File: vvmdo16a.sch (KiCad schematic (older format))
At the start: 18 parts, among them J1 517-N2510-6002RB, J2 517-N2520-6002RB, SW1 SW_Coded_SH-7010, U1 PCA9685PW, U2 ULN2803A, U3 ULN2803A

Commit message: More compact PCB
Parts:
- removed MK3, MK4: Mounting_Hole_PAD, Mounting_Holes:MountingHole_2.7mm_M2.5_DIN965_Pad, symbol mechanical:Mounting_Hole_PAD
- MK1, MK2: value Mounting_Hole_PAD -> M2.5
- SW1: value SW_Coded_SH-7010 -> 220ADC16
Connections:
- net A0: now reaches R1.1, SW1.1, U1.1 (A0)
- net A1: now reaches R2.1, SW1.2, U1.2 (A1)
- net A2: now reaches R3.1, SW1.4, U1.3 (A2)
- net A3: now reaches R4.1, SW1.8, U1.4 (A3)
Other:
- moved on the sheet: MK2
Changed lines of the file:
@@
 P 4250 5900
 F 0 "MK1" H 4350 5949 50  0000 L CNN
-F 1 "Mounting_Hole_PAD" H 4350 5858 50  0000 L CNN
+F 1 "M2.5" H 4350 5858 50  0000 L CNN
 F 2 "Mounting_Holes:MountingHole_2.7mm_M2.5_DIN965_Pad" H 4250 5900 50  0001 C CNN
 F 3 "" H 4250 5900 50  0001 C CNN
@@
 L mechanical:Mounting_Hole_PAD MK2
 U 1 1 5D014BC8
-P 4500 5900
-F 0 "MK2" H 4600 5949 50  0000 L CNN
-F 1 "Mounting_Hole_PAD" H 4600 5858 50  0000 L CNN
-F 2 "Mounting_Holes:MountingHole_2.7mm_M2.5_DIN965_Pad" H 4500 5900 50  0001 C CNN
-F 3 "" H 4500 5900 50  0001 C CNN
-	1    4500 5900
-	1    0    0    -1
-$EndComp
-$Comp
-L mechanical:Mounting_Hole_PAD MK3
-U 1 1 5D014C18
-P 4750 5900
-F 0 "MK3" H 4850 5949 50  0000 L CNN
-F 1 "Mounting_Hole_PAD" H 4850 5858 50  0000 L CNN
-F 2 "Mounting_Holes:MountingHole_2.7mm_M2.5_DIN965_Pad" H 4750 5900 50  0001 C CNN
-F 3 "" H 4750 5900 50  0001 C CNN
-	1    4750 5900
-	1    0    0    -1
-$EndComp
-$Comp
-L mechanical:Mounting_Hole_PAD MK4
-U 1 1 5D014E7E
-P 5000 5900
-F 0 "MK4" H 5100 5949 50  0000 L CNN
-F 1 "Mounting_Hole_PAD" H 5100 5858 50  0000 L CNN
-F 2 "Mounting_Holes:MountingHole_2.7mm_M2.5_DIN965_Pad" H 5000 5900 50  0001 C CNN
-F 3 "" H 5000 5900 50  0001 C CNN
-	1    5000 5900
+P 4550 5900
+F 0 "MK2" H 4650 5949 50  0000 L CNN
+F 1 "M2.5" H 4650 5858 50  0000 L CNN
+F 2 "Mounting_Holes:MountingHole_2.7mm_M2.5_DIN965_Pad" H 4550 5900 50  0001 C CNN
+F 3 "" H 4550 5900 50  0001 C CNN
+	1    4550 5900
 	1    0    0    -1
 $EndComp
@@
 L power:GND #PWR0107
 U 1 1 5D0210BD
-P 4650 6250
-F 0 "#PWR0107" H 4650 6000 50  0001 C CNN
-F 1 "GND" H 4655 6077 50  0000 C CNN
-F 2 "" H 4650 6250 50  0001 C CNN
-F 3 "" H 4650 6250 50  0001 C CNN
-	1    4650 6250
+P 4400 6250
+F 0 "#PWR0107" H 4400 6000 50  0001 C CNN
+F 1 "GND" H 4405 6077 50  0000 C CNN
+F 2 "" H 4400 6250 50  0001 C CNN
+F 3 "" H 4400 6250 50  0001 C CNN
+	1    4400 6250
 	1    0    0    -1
 $EndComp
 Wire Wire Line
 	4250 6000 4250 6100
-Wire Wire Line
-	4250 6100 4500 6100
-Wire Wire Line
-	4650 6100 4650 6250
-Wire Wire Line
-	4500 6000 4500 6100
-Connection ~ 4500 6100
-Wire Wire Line
-	4500 6100 4650 6100
-Wire Wire Line
-	4650 6100 4750 6100
-Wire Wire Line
-	4750 6100 4750 6000
-Connection ~ 4650 6100
-Wire Wire Line
-	4750 6100 5000 6100
-Wire Wire Line
-	5000 6100 5000 6000
-Connection ~ 4750 6100
 Wire Wire Line
 	7000 1900 8450 1900
@@
 P 1850 3750
 F 0 "SW1" H 1907 4217 50  0000 C CNN
-F 1 "SW_Coded_SH-7010" H 1907 4126 50  0000 C CNN
+F 1 "220ADC16" H 1907 4126 50  0000 C CNN
 F 2 "Buttons_Switches_THT:Nidec_Copal_SH-7010C" H 1550 3300 50  0001 L CNN
 F 3 "https://www.nidec-copal-electronics.com/e/catalog/switch/sh-7000.pdf" H 1850 3750 50  0001 C CNN
@@
 	1    0    0    -1
 $EndComp
+Text Label 3050 3650 0    50   ~ 0
+A0
+Text Label 3050 3750 0    50   ~ 0
+A1
+Text Label 3050 3850 0    50   ~ 0
+A2
+Text Label 3050 3950 0    50   ~ 0
+A3
+Wire Wire Line
+	4250 6100 4400 6100
+Wire Wire Line
+	4400 6100 4400 6250
+Wire Wire Line
+	4400 6100 4550 6100
+Wire Wire Line
+	4550 6100 4550 6000
 Wire Bus Line
 	9700 2050 9700 3450
@@
 Wire Bus Line
 	7550 2050 7550 4450
+Connection ~ 4400 6100
 $EndSCHEMATC

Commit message: Add seperate power rail input Label the board
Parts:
- added J3: Conn_02x01, Pin_Headers:Pin_Header_Straight_2x01_Pitch2.54mm, symbol conn:Conn_02x01
- added J4: Conn_02x01, TerminalBlocks_Phoenix:TerminalBlock_Phoenix_PT-3.5mm_2pol, symbol conn:Conn_02x01
- J1: value 517-N2510-6002RB -> 517-N2508-6002RB; footprint Connectors_IDC:IDC-Header_2x05_Pitch2.54mm_Straight -> Connector-IDC:IDC-Header_2x04_P2.54mm_Vertical; symbol conn:Conn_02x05_Odd_Even -> conn:Conn_02x04_Odd_Even
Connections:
- net +12V: now also J3.2 (Pin_2), J4.1 (Pin_1); no longer J1.7 (Pin_7), J1.8 (Pin_8)
- net +3V3: now also J1.5 (Pin_5), J1.6 (Pin_6); no longer J1.1 (Pin_1), J1.2 (Pin_2)
- net GND: now also J1.1 (Pin_1), J1.2 (Pin_2), J4.2 (Pin_2); no longer J1.10 (Pin_10), J1.9 (Pin_9)
- net SCL: now also J1.3 (Pin_3); no longer J1.4 (Pin_4)
- net SDA: now also J1.4 (Pin_4); no longer J1.3 (Pin_3)
- new net +12VIN: J1.7 (Pin_7), J1.8 (Pin_8), J3.1 (Pin_1)
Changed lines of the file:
@@
 O16
 $Comp
-L conn:Conn_02x05_Odd_Even J1
+L conn:Conn_02x04_Odd_Even J1
 U 1 1 5CD0D077
-P 1950 2850
-F 0 "J1" H 2000 3267 50  0000 C CNN
-F 1 "517-N2510-6002RB" H 2000 3176 50  0000 C CNN
-F 2 "Connectors_IDC:IDC-Header_2x05_Pitch2.54mm_Straight" H 1950 2850 50  0001 C CNN
-F 3 "~" H 1950 2850 50  0001 C CNN
-	1    1950 2850
-	1    0    0    -1
+P 2250 2350
+F 0 "J1" H 2300 2767 50  0000 C CNN
+F 1 "517-N2508-6002RB" H 2300 2676 50  0000 C CNN
+F 2 "Connector-IDC:IDC-Header_2x04_P2.54mm_Vertical" H 2250 2350 50  0001 C CNN
+F 3 "~" H 2250 2350 50  0001 C CNN
+	1    2250 2350
+	-1   0    0    1
 $EndComp
 Wire Wire Line
@@
 $EndComp
 Wire Wire Line
-	3950 1750 3950 2000
-Wire Wire Line
-	3250 2750 2250 2750
-Wire Wire Line
-	3250 2850 2750 2850
-Wire Wire Line
-	2750 2850 2750 2350
-Wire Wire Line
-	2750 2350 1550 2350
-Wire Wire Line
-	1550 2350 1550 2750
-Wire Wire Line
-	1550 2750 1750 2750
-Wire Wire Line
-	1750 2650 1350 2650
-Wire Wire Line
-	1350 2650 1350 2000
-Wire Wire Line
-	1350 2000 2450 2000
-Connection ~ 3950 2000
-Wire Wire Line
-	3950 2000 3950 2450
-Wire Wire Line
 	3250 4150 3150 4150
 Wire Wire Line
@@
 Connection ~ 2700 4950
 Wire Wire Line
-	2250 2650 2450 2650
-Wire Wire Line
-	2450 2650 2450 2000
-Connection ~ 2450 2000
-Wire Wire Line
-	2450 2000 3950 2000
-Wire Wire Line
-	2250 3050 2350 3050
-Wire Wire Line
 	2350 3050 2350 4950
 Wire Wire Line
@@
 Connection ~ 2550 4950
 Wire Wire Line
-	1750 3050 1450 3050
-Wire Wire Line
-	1450 3050 1450 4950
-Wire Wire Line
 	1450 4950 2350 4950
 Connection ~ 2350 4950
-Wire Wire Line
-	2250 2950 2550 2950
-Wire Wire Line
-	2550 2950 2550 1900
-Wire Wire Line
-	2550 1900 1450 1900
-Wire Wire Line
-	1450 1900 1450 2950
-Wire Wire Line
-	1450 2950 1750 2950
-Wire Wire Line
-	2550 1900 7000 1900
-Connection ~ 2550 1900
 Connection ~ 7000 1900
 Wire Wire Line
 	7000 1900 7000 1650
-Text Label 2300 2750 0    50   ~ 0
+Text Label 3000 2750 0    50   ~ 0
 SCL
-Text Label 1600 2750 0    50   ~ 0
+Text Label 3000 2850 0    50   ~ 0
 SDA
-Text Label 2300 2950 0    50   ~ 0
-+12V
 $Comp
 L device:C C1
@@
 Wire Wire Line
 	3250 3050 3000 3050
-Connection ~ 2350 3050
 Wire Wire Line
 	3250 2950 3000 2950
@@
 Connection ~ 3000 3050
 Wire Wire Line
-	3000 3050 2350 3050
+	3000 3050 2500 3050
 $Comp
 L device:C C3
@@
 	2250 3300 1350 3300
 Wire Wire Line
-	1350 3300 1350 2650
-Connection ~ 1350 2650
-Wire Wire Line
 	1350 4150 1350 3300
-Connection ~ 1350 3300
 Wire Wire Line
 	2250 3950 3000 3950
@@
 Wire Wire Line
 	4550 6100 4550 6000
+Connection ~ 4400 6100
+$Comp
+L power:+3.3V #PWR0108
+U 1 1 5CEB80C2
+P 1350 3150
+F 0 "#PWR0108" H 1350 3000 50  0001 C CNN
+F 1 "+3.3V" H 1365 3323 50  0000 C CNN
+F 2 "" H 1350 3150 50  0001 C CNN
+F 3 "" H 1350 3150 50  0001 C CNN
+	1    1350 3150
+	1    0    0    -1
+$EndComp
+Wire Wire Line
+	1350 3150 1350 3300
+Connection ~ 1350 3300
+Wire Wire Line
+	2900 2750 2900 2350
+Wire Wire Line
+	2900 2350 2450 2350
+Wire Wire Line
+	2900 2750 3250 2750
+Wire Wire Line
+	1700 2850 1700 2350
+Wire Wire Line
+	1700 2350 1950 2350
+Wire Wire Line
+	1700 2850 3250 2850
+Wire Wire Line
+	1950 2450 1800 2450
+Wire Wire Line
+	1800 2450 1800 2600
+Wire Wire Line
+	1800 2600 2500 2600
+Wire Wire Line
+	2500 2600 2500 3050
+Connection ~ 2500 3050
+Wire Wire Line
+	2500 3050 2350 3050
+Wire Wire Line
+	2450 2450 2500 2450
+Wire Wire Line
+	2500 2450 2500 2500
+Connection ~ 2500 2600
+Wire Wire Line
+	1950 2250 1700 2250
+Wire Wire Line
+	1700 2250 1700 1750
+Wire Wire Line
+	1700 1750 2500 1750
+Connection ~ 3950 1750
+Wire Wire Line
+	3950 1750 3950 2450
+Wire Wire Line
+	2450 2250 2500 2250
+Wire Wire Line
+	2500 2250 2500 1750
+Connection ~ 2500 1750
+Wire Wire Line
+	2500 1750 3950 1750
+Wire Wire Line
+	2450 2150 2600 2150
+Wire Wire Line
+	2600 2150 2600 2000
+$Comp
+L conn:Conn_02x01 J3
+U 1 1 5CF8667A
+P 2900 2000
+F 0 "J3" H 2950 2217 50  0000 C CNN
+F 1 "Conn_02x01" H 2950 2126 50  0000 C CNN
+F 2 "Pin_Headers:Pin_Header_Straight_2x01_Pitch2.54mm" H 2900 2000 50  0001 C CNN
+F 3 "~" H 2900 2000 50  0001 C CNN
+	1    2900 2000
+	1    0    0    -1
+$EndComp
+Wire Wire Line
+	2700 2000 2600 2000
+Wire Wire Line
+	2600 2000 1850 2000
+Wire Wire Line
+	1850 2000 1850 2150
+Wire Wire Line
+	1850 2150 1950 2150
+Connection ~ 2600 2000
+$Comp
+L conn:Conn_02x01 J4
+U 1 1 5CF9F54F
+P 3300 2200
+F 0 "J4" V 3304 2280 50  0000 L CNN
+F 1 "Conn_02x01" V 3395 2280 50  0000 L CNN
+F 2 "TerminalBlocks_Phoenix:TerminalBlock_Phoenix_PT-3.5mm_2pol" H 3300 2200 50  0001 C CNN
+F 3 "~" H 3300 2200 50  0001 C CNN
+	1    3300 2200
+	0    1    1    0
+$EndComp
+Wire Wire Line
+	3200 2000 3300 2000
+Wire Wire Line
+	3300 2000 3300 1900
+Wire Wire Line
+	3300 1900 7000 1900
+Connection ~ 3300 2000
+Wire Wire Line
+	3300 2500 2500 2500
 Wire Bus Line
 	9700 2050 9700 3450
@@
 Wire Bus Line
 	7550 2050 7550 4450
-Connection ~ 4400 6100
+Connection ~ 2500 2500
+Wire Wire Line
+	2500 2500 2500 2600
+Text Label 2000 2000 0    50   ~ 0
++12VIN
 $EndSCHEMATC

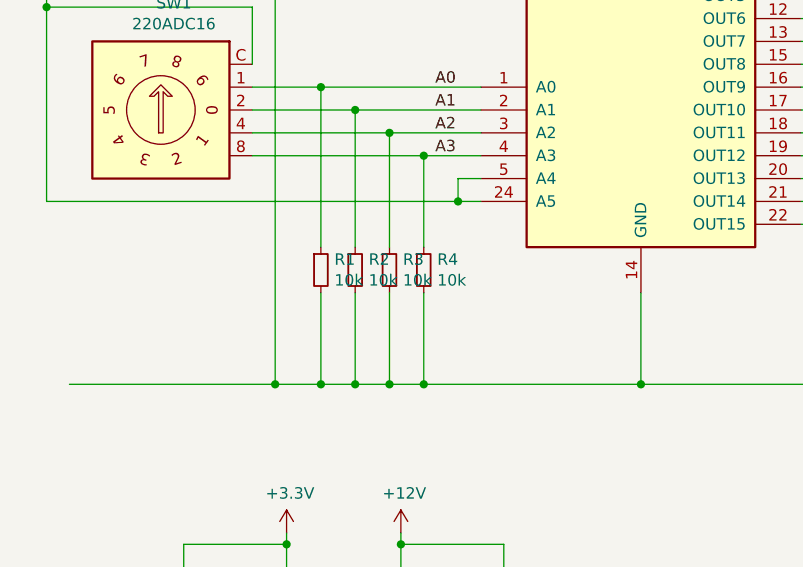
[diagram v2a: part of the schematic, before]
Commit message: Tie A4 to GND instead of +3V3
This selects addresses 0x60-0x6f for the IO controller.

Fixes #1
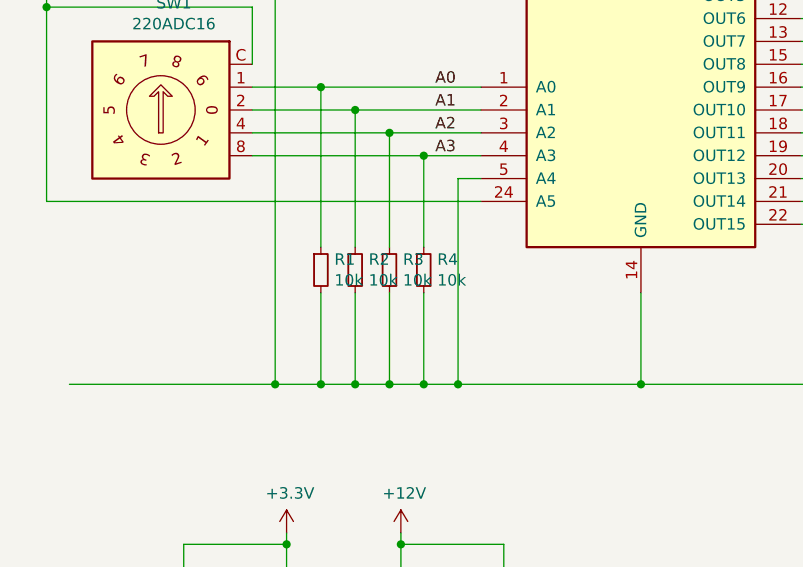
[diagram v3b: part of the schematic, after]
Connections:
- net +3V3: no longer U1.5 (A4)
- net GND: now also U1.5 (A4)
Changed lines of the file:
@@
 $EndComp
-Wire Wire Line
-	3250 4150 3150 4150
 Wire Wire Line
 	3250 4050 3150 4050
-Wire Wire Line
-	3150 4050 3150 4150
-Connection ~ 3150 4150
-Wire Wire Line
-	3150 4150 1350 4150
 Wire Wire Line
 	3000 4350 3000 3950
@@
 	3000 4550 3000 4950
 Wire Wire Line
-	3000 4950 3950 4950
+	3000 4950 3150 4950
 Connection ~ 3950 4950
 Wire Wire Line
@@
 Wire Wire Line
 	3300 2500 2500 2500
+Connection ~ 2500 2500
+Wire Wire Line
+	2500 2500 2500 2600
+Text Label 2000 2000 0    50   ~ 0
++12VIN
+Wire Wire Line
+	1350 4150 3250 4150
+Wire Wire Line
+	3150 4050 3150 4950
 Wire Bus Line
 	9700 2050 9700 3450
@@
 Wire Bus Line
 	7550 2050 7550 4450
-Connection ~ 2500 2500
-Wire Wire Line
-	2500 2500 2500 2600
-Text Label 2000 2000 0    50   ~ 0
-+12VIN
+Connection ~ 3150 4950
+Wire Wire Line
+	3150 4950 3950 4950
 $EndSCHEMATC
